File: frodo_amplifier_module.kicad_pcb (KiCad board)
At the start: 2 copper layers, 27 x 20 mm, 24 parts, among them IC1 INA826AID, J1 JST-GH, J2 JST-GH, U1 NCS20071SN

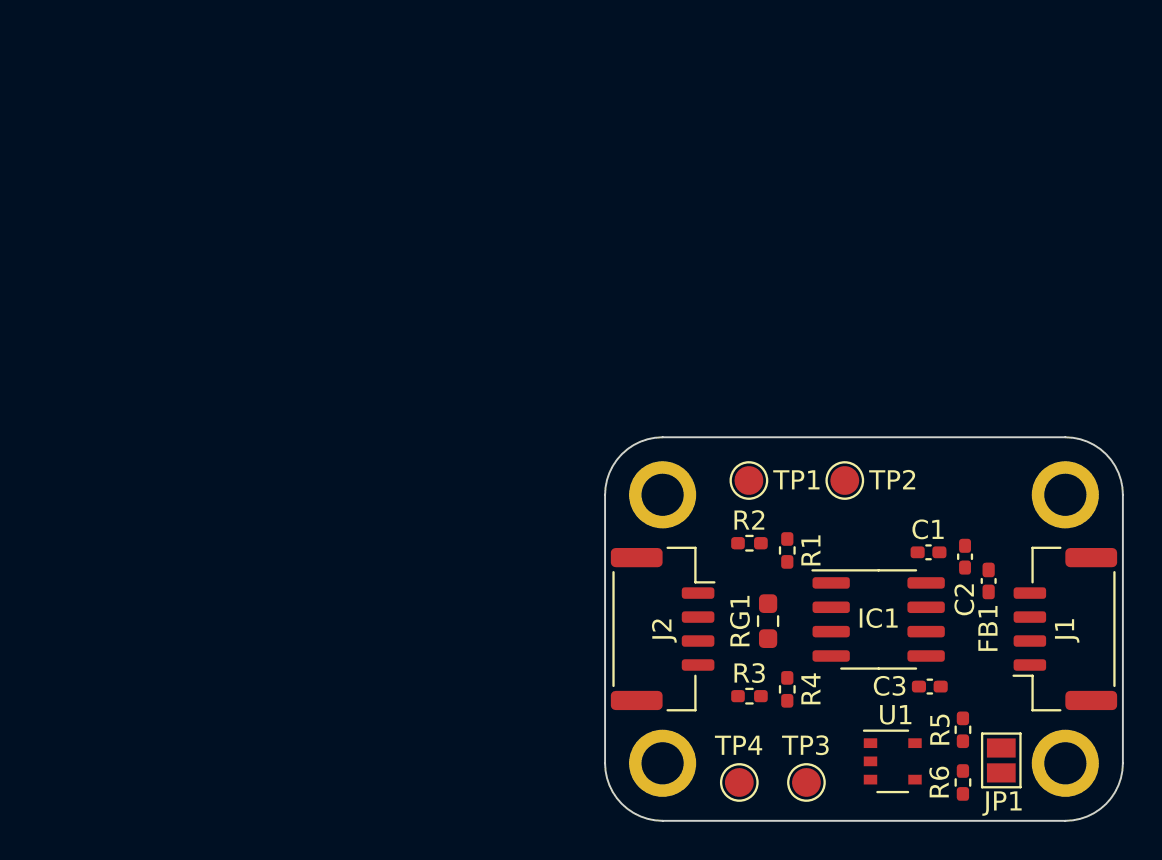
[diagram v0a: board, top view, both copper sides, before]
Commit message: updated amplifier module, removed mounting holes and routed the pcb
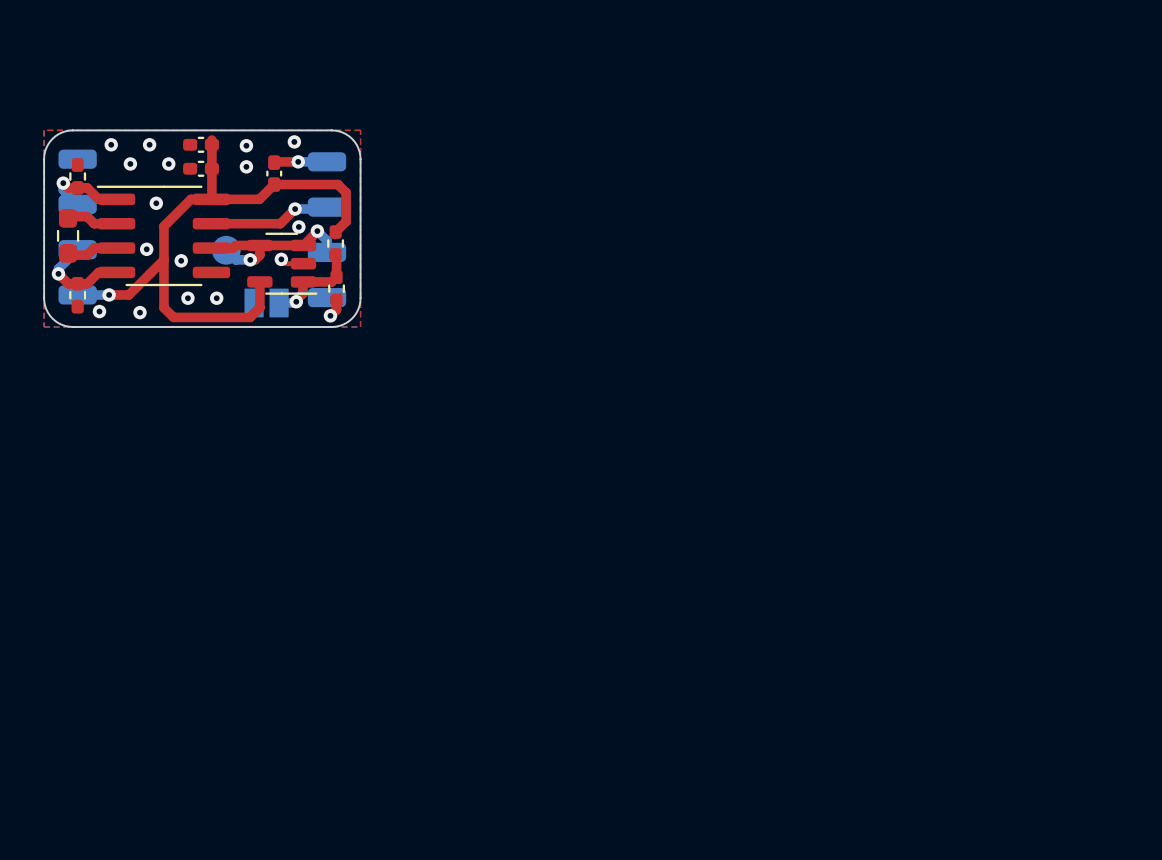
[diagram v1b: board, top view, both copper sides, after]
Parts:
- removed C3: 100n, Capacitor_SMD:C_0402_1005Metric_Pad0.74x0.62mm_HandSolder
- removed H1, H2, H3, H4: MountingHole, MountingHole:MountingHole_2.2mm_M2_ISO7380_Pad
- removed R5, R6: 10k, Resistor_SMD:R_0402_1005Metric_Pad0.72x0.64mm_HandSolder
- removed TP2, TP3, TP4: TestPoint, TestPoint:TestPoint_Pad_D1.5mm
- removed U1: NCS20071SN, Package_SO:TSOP-5_1.65x3.05mm_P0.95mm
- added IC2: AS321KTR-G1, Package_TO_SOT_SMD:SOT-23-5, F.Cu at (85.6, 53.5)
- added J3: Conn_01x01_Socket, Connector_Wire:SolderWirePad_1x01_SMD_1x2mm, B.Cu at (88.0, 52.9)
- added J4: Conn_01x01_Socket, Connector_Wire:SolderWirePad_1x01_SMD_1x2mm, B.Cu at (88.0, 55.2)
- added J5: Conn_01x01_Socket, Connector_Wire:SolderWirePad_1x01_SMD_1x2mm, B.Cu at (75.0, 55.1)
- added J6: Conn_01x01_Socket, Connector_Wire:SolderWirePad_1x01_SMD_1x2mm, B.Cu at (75.0, 52.7)
- added J7: Conn_01x01_Socket, Connector_Wire:SolderWirePad_1x01_SMD_1x2mm, B.Cu at (75.0, 50.4)
- added J8: Conn_01x01_Socket, Connector_Wire:SolderWirePad_1x01_SMD_1x2mm, B.Cu at (75.0, 48.0)
- J1, J2: value JST-GH -> Conn_01x01_Socket; footprint Connector_JST:JST_GH_SM04B-GHS-TB_1x04-1MP_P1.25mm_Horizontal -> Connector_Wire:SolderWirePad_1x01_SMD_1x2mm; moved to B.Cu
- JP1, TP1: moved to B.Cu
- R2: value 10k -> 47k
- R4: value 47k -> 10k
- moved J1 45.6 mm to (88.0, 48.1), turned to -90 degrees
- moved C2 45.3 mm to (81.4, 47.2), turned to 180 degrees
- moved JP1 45.1 mm to (84.8, 55.5), turned to 0 degrees
- moved C1 42.9 mm to (81.4, 48.5), turned to 180 degrees
- moved FB1 42.9 mm to (85.2, 48.8), turned to -90 degrees
- moved IC1 42.3 mm to (79.5, 52.0)
- moved R1 41.8 mm to (75.0, 48.9)
- moved RG1 41.7 mm to (74.5, 52.0)
- moved R2 37.3 mm to (75.0, 55.1), turned to 90 degrees
- moved R3 32.0 mm to (88.5, 52.4), turned to 90 degrees
- moved R4 31.4 mm to (88.5, 54.8)
- moved TP1 29.8 mm to (82.8, 52.8), turned to 180 degrees
- moved J2 28.1 mm to (88.0, 50.5)
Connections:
- FB1 pad 1: Net-(J1-Pin_4) -> Net-(J1-Pin_1)
- IC1 pad 1: Net-(IC1--IN) -> -IN
- IC1 pad 4: Net-(IC1-+IN) -> +IN
- J1 pad 1: GND -> Net-(J1-Pin_1)
- J2 pad 1: GND -> out
- JP1 pad 2: Net-(JP1-B) -> Net-(IC2-INPUT_+)
- R1 pad 1: Net-(IC1--IN) -> -IN
- R2 pad 1: -IN -> GND
- R2 pad 2: Net-(IC1--IN) -> +IN
- R3 pad 1: +IN -> Net-(IC2-INPUT_+)
- R3 pad 2: Net-(IC1-+IN) -> VDD
- R4 pad 2: Net-(IC1-+IN) -> Net-(IC2-INPUT_+)
- TP1 pad 1: Net-(IC1--IN) -> ref
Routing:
- net VDD: track 0.00 -> 32.2 mm, vias 0 -> 1
- net ref: track 0.00 -> 9.78 mm, vias 0 -> 2
- net out: track 0.00 -> 6.38 mm, vias 0 -> 1
- net +IN: track 0.00 -> 5.16 mm, vias 0 -> 1
- net Net-(IC2-INPUT_+): track 0.00 -> 4.80 mm, vias 0 -> 1
- net -IN: track 0.00 -> 4.55 mm, vias 0 -> 1
- net Net-(IC1-RG_2): track 0.00 -> 2.71 mm
- net Net-(IC1-RG_1): track 0.00 -> 2.71 mm
- net Net-(J1-Pin_1): track 0.00 -> 2.52 mm, vias 0 -> 1
- net GND: track 0.00 -> 1.95 mm, vias 0 -> 17
- added copper zone on B.Cu, net GND
- added copper zone on F.Cu, net GND
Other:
- board size 27 x 20 mm -> 16.5 x 10.2 mm

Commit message: updated stuff
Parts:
- removed TP1: TestPoint, TestPoint:TestPoint_Pad_D1.5mm
- added H1: MountingHole, MountingHole:MountingHole_3.2mm_M3, F.Cu at (81.5, 44.0)
- added H2: MountingHole, MountingHole:MountingHole_3.2mm_M3, F.Cu at (81.5, 59.2)
- JP1: value SolderJumper_2_Open -> SolderJumper_3_Open; footprint Jumper:SolderJumper-2_P1.3mm_Open_Pad1.0x1.5mm -> Jumper:SolderJumper-3_P1.3mm_Open_RoundedPad1.0x1.5mm_NumberLabels
- moved J6 4.94 mm to (75.0, 47.8)
- moved J7 2.50 mm to (75.0, 52.9)
- moved J8 2.32 mm to (75.0, 50.3)
- moved JP1 1.31 mm to (85.0, 54.2), turned to -90 degrees
- moved J5 0.32 mm to (75.0, 55.4)
- moved RG1 0.20 mm to (74.7, 52.0)
- moved C2 0.15 mm to (81.4, 47.4)
- moved C1 0.10 mm to (81.4, 48.6)
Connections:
- R3 pad 1: Net-(IC2-INPUT_+) -> Net-(JP1-B)
- R4 pad 2: Net-(IC2-INPUT_+) -> Net-(JP1-B)
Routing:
- net Net-(JP1-B): track 0.00 -> 6.36 mm, vias 0 -> 1
- net +IN: track 5.16 -> 10.8 mm
- net -IN: track 4.55 -> 9.44 mm
- net ref: track 9.78 -> 7.58 mm, vias 2 -> 1
- net GND: track 1.95 -> 4.10 mm
- net VDD: track 32.2 -> 31.2 mm
- net Net-(IC2-INPUT_+): track 4.80 -> 4.10 mm
- net (no net): vias 0 -> 14
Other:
- board size 16.5 x 10.2 mm -> 16.5 x 19.8 mm
- board text added: "1 for gnd 3 for ref"
- board text added: "o+"
- board text added: "ref"
- board text added: "s+"
- board text added: "s-"
- board text added: "u+"
- board text added: "u-"

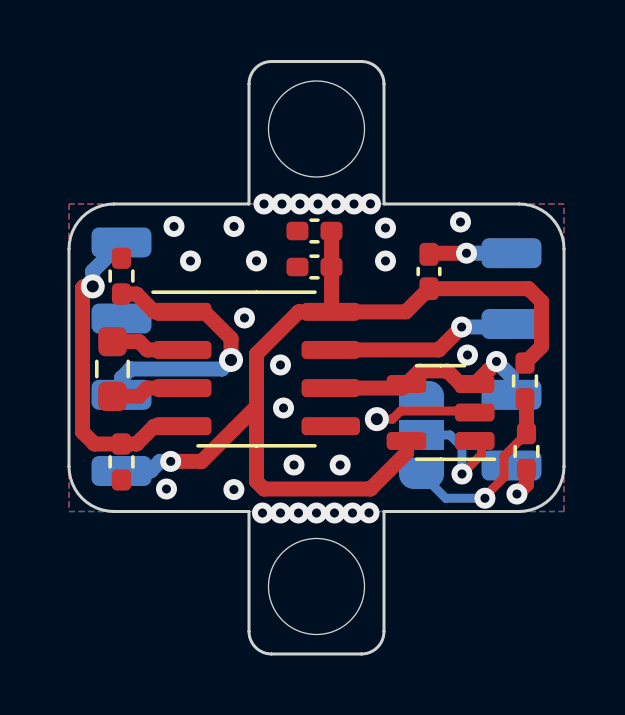
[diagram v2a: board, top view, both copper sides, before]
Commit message: fixed soulder jumper, added mousbites
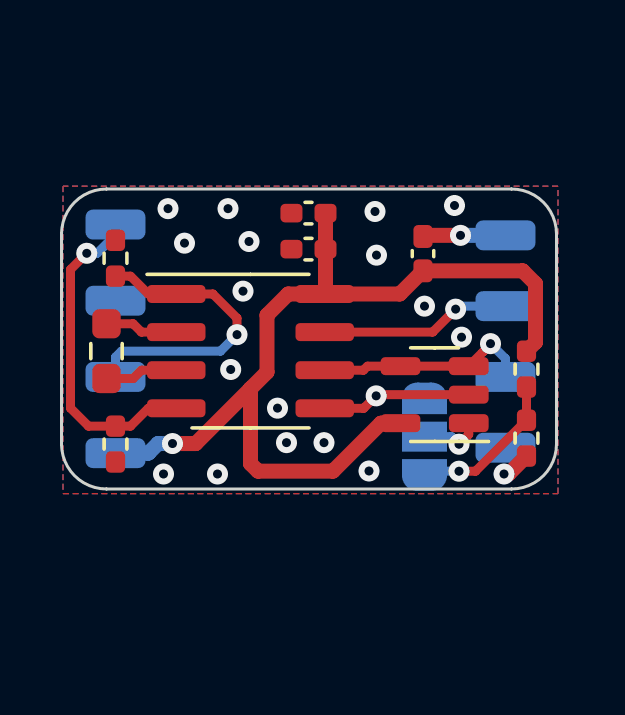
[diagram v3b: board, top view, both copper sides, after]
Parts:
- removed H1, H2: MountingHole, MountingHole:MountingHole_3.2mm_M3
- moved IC2 0.63 mm to (85.4, 52.9)
- moved R1 0.63 mm to (74.8, 48.3)
- moved C1 0.63 mm to (81.2, 48.0)
- moved C2 0.63 mm to (81.2, 46.8)
- moved FB1 0.63 mm to (85.0, 48.2)
- moved IC1 0.63 mm to (79.3, 51.4)
- moved J1 0.63 mm to (87.8, 47.5)
- moved J2 0.63 mm to (87.8, 49.9)
- moved J3 0.63 mm to (87.8, 52.3)
- moved J4 0.63 mm to (87.8, 54.6)
- moved J5 0.63 mm to (74.8, 54.8)
- moved J6 0.63 mm to (74.8, 47.2)
- moved J7 0.63 mm to (74.8, 52.3)
- moved J8 0.63 mm to (74.8, 49.7)
- moved R2 0.63 mm to (74.8, 54.5)
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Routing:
- net Net-(IC2-INPUT_+): track 4.10 -> 2.09 mm
- net GND: track 4.10 -> 5.93 mm, vias 17 -> 19
- net Net-(JP1-B): track 6.36 -> 5.22 mm
- net -IN: track 9.44 -> 10.2 mm
- net (no net): vias 14 -> 0
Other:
- board size 16.5 x 19.8 mm -> 16.5 x 10 mm
